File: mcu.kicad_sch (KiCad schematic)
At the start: 24 parts, among them SW1 SW_Push, SW2 SW_Push, U1 RP2040, U2 W25Q128JVS, Y1 Crystal_GND24

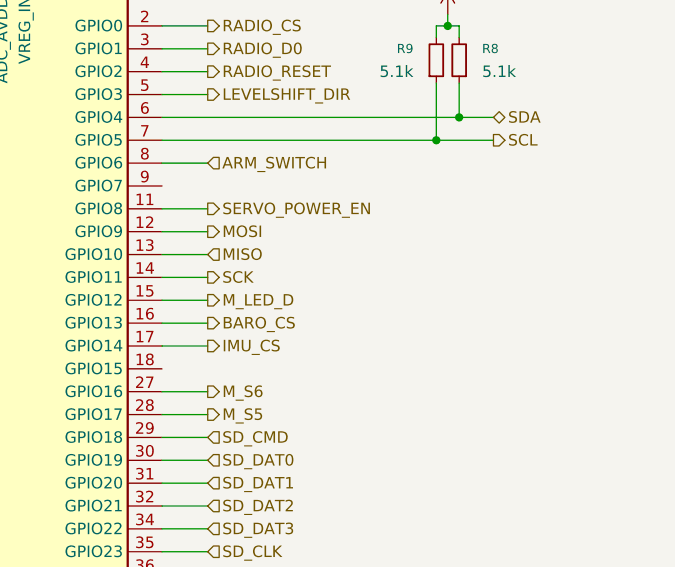
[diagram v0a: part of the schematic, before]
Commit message: switched around some footprints, added expansion header
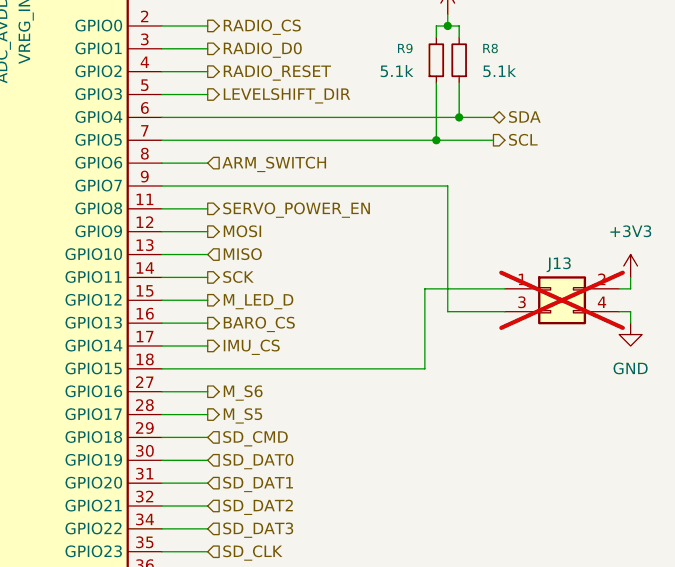
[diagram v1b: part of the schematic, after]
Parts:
- added J13: Conn_02x02_Odd_Even, Connector_PinHeader_1.27mm:PinHeader_2x02_P1.27mm_Vertical, symbol Connector_Generic:Conn_02x02_Odd_Even
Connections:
- net +3V3: now also J13.2 (Pin_2)
- net GND: now also J13.4 (Pin_4)
- net at U1.18 (GPIO15): now also J13.1 (Pin_1)
- net at U1.9 (GPIO7): now also J13.3 (Pin_3)

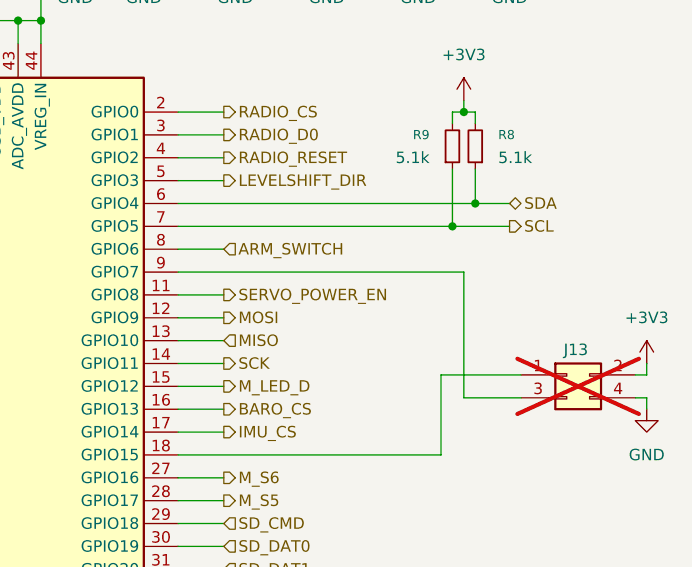
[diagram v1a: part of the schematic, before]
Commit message: switched to global labels for SPI and I2C, added labels for servos
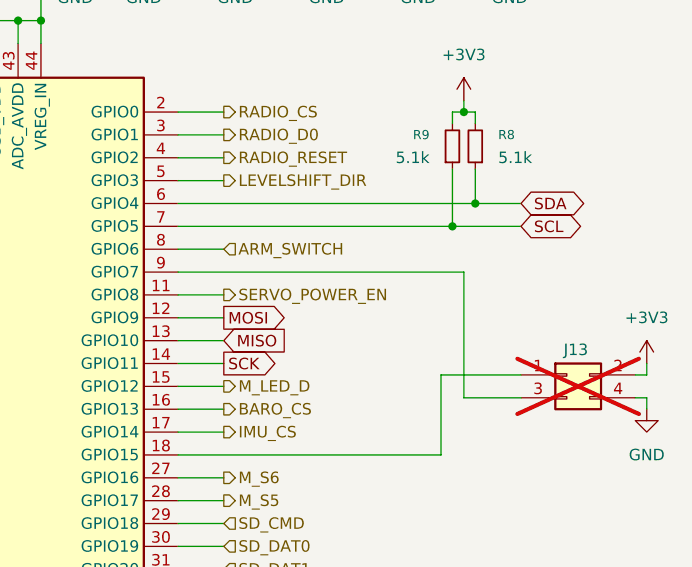
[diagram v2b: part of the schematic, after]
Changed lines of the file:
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@@
 	(wire
 		(pts
-			(xy 226.06 54.61) (xy 229.87 54.61)
+			(xy 226.06 54.61) (xy 231.14 54.61)
 		)
 		(stroke
@@
 	(wire
 		(pts
-			(xy 223.52 57.15) (xy 229.87 57.15)
+			(xy 223.52 57.15) (xy 231.14 57.15)
 		)
 		(stroke
@@
 			)
 			(justify right bottom)
+		)
+	)
+	(global_label "SDA"
+		(shape bidirectional)
+		(at 231.14 54.61 0)
+		(fields_autoplaced yes)
+		(effects
+			(font
+				(size 1.27 1.27)
+			)
+			(justify left)
+		)
+		(property "Intersheetrefs" "${INTERSHEET_REFS}"
+			(at 238.8046 54.61 0)
+			(effects
+				(font
+					(size 1.27 1.27)
+				)
+				(justify left)
+				(hide yes)
+			)
+		)
+	)
+	(global_label "SCK"
+		(shape output)
+		(at 198.12 72.39 0)
+		(fields_autoplaced yes)
+		(effects
+			(font
+				(size 1.27 1.27)
+			)
+			(justify left)
+		)
+		(property "Intersheetrefs" "${INTERSHEET_REFS}"
+			(at 204.8547 72.39 0)
+			(effects
+				(font
+					(size 1.27 1.27)
+				)
+				(justify left)
+				(hide yes)
+			)
+		)
+	)
+	(global_label "SCL"
+		(shape bidirectional)
+		(at 231.14 57.15 0)
+		(fields_autoplaced yes)
+		(effects
+			(font
+				(size 1.27 1.27)
+			)
+			(justify left)
+		)
+		(property "Intersheetrefs" "${INTERSHEET_REFS}"
+			(at 238.7441 57.15 0)
+			(effects
+				(font
+					(size 1.27 1.27)
+				)
+				(justify left)
+				(hide yes)
+			)
+		)
+	)
+	(global_label "MOSI"
+		(shape output)
+		(at 198.12 67.31 0)
+		(fields_autoplaced yes)
+		(effects
+			(font
+				(size 1.27 1.27)
+			)
+			(justify left)
+		)
+		(property "Intersheetrefs" "${INTERSHEET_REFS}"
+			(at 205.7014 67.31 0)
+			(effects
+				(font
+					(size 1.27 1.27)
+				)
+				(justify left)
+				(hide yes)
+			)
+		)
+	)
+	(global_label "MISO"
+		(shape input)
+		(at 198.12 69.85 0)
+		(fields_autoplaced yes)
+		(effects
+			(font
+				(size 1.27 1.27)
+			)
+			(justify left)
+		)
+		(property "Intersheetrefs" "${INTERSHEET_REFS}"
+			(at 205.7014 69.85 0)
+			(effects
+				(font
+					(size 1.27 1.27)
+				)
+				(justify left)
+				(hide yes)
+			)
 		)
 	)
@@
 		)
 	)
-	(hierarchical_label "MOSI"
-		(shape output)
-		(at 198.12 67.31 0)
-		(effects
-			(font
-				(size 1.27 1.27)
-			)
-			(justify left)
-		)
-	)
 	(hierarchical_label "M_S2"
 		(shape output)
@@
 		)
 	)
-	(hierarchical_label "SCK"
-		(shape output)
-		(at 198.12 72.39 0)
-		(effects
-			(font
-				(size 1.27 1.27)
-			)
-			(justify left)
-		)
-	)
 	(hierarchical_label "LEVELSHIFT_DIR"
 		(shape output)
@@
 		)
 	)
-	(hierarchical_label "MISO"
-		(shape input)
-		(at 198.12 69.85 0)
-		(effects
-			(font
-				(size 1.27 1.27)
-			)
-			(justify left)
-		)
-	)
 	(hierarchical_label "M_S6"
 		(shape output)
@@
 		(effects
 			(font
-				(size 1.27 1.27)
-			)
-			(justify left)
-		)
-	)
-	(hierarchical_label "SCL"
-		(shape output)
-		(at 229.87 57.15 0)
-		(effects
-			(font
-				(size 1.27 1.27)
-			)
-			(justify left)
-		)
-	)
-	(hierarchical_label "SDA"
-		(shape bidirectional)
-		(at 229.87 54.61 0)
-		(effects
-			(font

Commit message: add reset pullup...
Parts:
- added R14: 5.1k, Resistor_SMD:R_0402_1005Metric, symbol Device:R_Small
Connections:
- net +3V3: now also R14.2
- net ~{RESET}: now also R14.1
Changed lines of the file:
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@@
 	)
 	(junction
+		(at 124.46 44.45)
+		(diameter 0)
+		(color 0 0 0 0)
+	)
+	(junction
 		(at 153.67 25.4)
 		(diameter 0)
@@
 	(wire
 		(pts
+			(xy 124.46 36.83) (xy 124.46 38.1)
+		)
+		(stroke
+			(width 0)
+			(type default)
+		)
+	)
+	(wire
+		(pts
 			(xy 130.81 77.47) (xy 130.81 64.77)
 		)
@@
 	(wire
 		(pts
+			(xy 124.46 44.45) (xy 142.24 44.45)
+		)
+		(stroke
+			(width 0)
+			(type default)
+		)
+	)
+	(wire
+		(pts
 			(xy 130.81 52.07) (xy 134.62 52.07)
 		)
@@
 	(wire
 		(pts
-			(xy 118.11 44.45) (xy 142.24 44.45)
+			(xy 118.11 44.45) (xy 124.46 44.45)
 		)
 		(stroke
@@
 	(wire
 		(pts
+			(xy 124.46 43.18) (xy 124.46 44.45)
+		)
+		(stroke
+			(width 0)
+			(type default)
+		)
+	)
+	(wire
+		(pts
 			(xy 222.25 73.66) (xy 222.25 82.55)
 		)
@@
 	(symbol
 		(lib_id "Device:R_Small")
+		(at 124.46 40.64 0)
+		(mirror x)
+		(unit 1)
+		(exclude_from_sim no)
+		(in_bom yes)
+		(on_board yes)
+		(dnp no)
+		(property "Reference" "R14"
+			(at 121.92 39.3699 0)
+			(effects
+				(font
+					(size 1.016 1.016)
+				)
+				(justify right)
+			)
+		)
+		(property "Value" "5.1k"
+			(at 121.92 41.9099 0)
+			(effects
+				(font
+					(size 1.27 1.27)
+				)
+				(justify right)
+			)
+		)
+		(property "Footprint" "Resistor_SMD:R_0402_1005Metric"
+			(at 124.46 40.64 0)
+			(effects
+				(font
+					(size 1.27 1.27)
+				)
+				(hide yes)
+			)
+		)
+		(property "Datasheet" "~"
+			(at 124.46 40.64 0)
+			(effects
+				(font
+					(size 1.27 1.27)
+				)
+				(hide yes)
+			)
+		)
+		(property "Description" "Resistor, small symbol"
+			(at 124.46 40.64 0)
+			(effects
+				(font
+					(size 1.27 1.27)
+				)
+				(hide yes)
+			)
+		)
+		(property "LCSC" "C25905"
+			(at 124.46 40.64 0)
+			(effects
+				(font
+					(size 1.27 1.27)
+				)
+				(hide yes)
+			)
+		)
+		(property "digikey" ""
+			(at 124.46 40.64 0)
+			(effects
+				(font
+					(size 1.27 1.27)
+				)
+				(hide yes)
+			)
+		)
+		(pin "2"
+		)
+		(pin "1"
+		)
+		(instances
+			(project "beavs-sketch-0"
+				(path "/49232f62-a438-4b3e-9be5-c2b3074d8de1/41e54b18-0bb2-4af3-8e30-a27cf4650be3"
+					(reference "R14")
+					(unit 1)
+				)
+			)
+		)
+	)
+	(symbol
+		(lib_id "Device:R_Small")
 		(at 223.52 48.26 0)
 		(mirror x)
@@
 					(unit 1)
 				)
+			)
+		)
+	)
+	(symbol
+		(lib_id "power:+3V3")
+		(at 124.46 36.83 0)
+		(unit 1)
+		(exclude_from_sim no)
+		(in_bom yes)
+		(on_board yes)
+		(dnp no)
+		(fields_autoplaced yes)
+		(property "Reference" "#PWR0134"
+			(at 124.46 40.64 0)
+			(effects
+				(font
+					(size 1.27 1.27)
+				)
+				(hide yes)
+			)
+		)
+		(property "Value" "+3V3"
+			(at 124.46 31.75 0)
+			(effects
+				(font
+					(size 1.27 1.27)
+				)
+			)
+		)
+		(property "Footprint" ""
+			(at 124.46 36.83 0)
+			(effects
+				(font
+					(size 1.27 1.27)
+				)
+				(hide yes)
+			)
+		)
+		(property "Datasheet" ""
+			(at 124.46 36.83 0)
+			(effects
+				(font
+					(size 1.27 1.27)
+				)
+				(hide yes)
+			)
+		)
+		(property "Description" "Power symbol creates a global label with name \"+3V3\""
+			(at 124.46 36.83 0)
+			(effects
+				(font
+					(size 1.27 1.27)
+				)
+				(hide yes)
+			)
+		)
+		(pin "1"
+		)
+		(instances
+			(project "beavs-sketch-0"
+				(path "/49232f62-a438-4b3e-9be5-c2b3074d8de1/41e54b18-0bb2-4af3-8e30-a27cf4650be3"
+					(reference "#PWR0134")
+					(unit 1)
+				)

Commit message: various tweaks
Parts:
- added TP1, TP2: TestPoint, TestPoint:TestPoint_Pad_D1.0mm, symbol Connector:TestPoint
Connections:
- net GND: now also U1.19 (TESTEN)
- net at U1.24 (SWCLK): now also TP1.1
- net at U1.25 (SWD): now also TP2.1
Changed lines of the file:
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@@
 	(wire
 		(pts
+			(xy 140.97 120.65) (xy 140.97 121.92)
+		)
+		(stroke
+			(width 0)
+			(type default)
+		)
+	)
+	(wire
+		(pts
 			(xy 175.26 34.29) (xy 175.26 36.83)
 		)
@@
 	(wire
 		(pts
+			(xy 142.24 120.65) (xy 140.97 120.65)
+		)
+		(stroke
+			(width 0)
+			(type default)
+		)
+	)
+	(wire
+		(pts
 			(xy 193.04 72.39) (xy 198.12 72.39)
 		)
@@
 	)
 	(symbol
+		(lib_id "Connector:TestPoint")
+		(at 142.24 110.49 90)
+		(unit 1)
+		(exclude_from_sim no)
+		(in_bom yes)
+		(on_board yes)
+		(dnp no)
+		(fields_autoplaced yes)
+		(property "Reference" "TP1"
+			(at 138.938 105.41 90)
+			(effects
+				(font
+					(size 1.27 1.27)
+				)
+			)
+		)
+		(property "Value" "TestPoint"
+			(at 138.938 107.95 90)
+			(effects
+				(font
+					(size 1.27 1.27)
+				)
+			)
+		)
+		(property "Footprint" "TestPoint:TestPoint_Pad_D1.0mm"
+			(at 142.24 105.41 0)
+			(effects
+				(font
+					(size 1.27 1.27)
+				)
+				(hide yes)
+			)
+		)
+		(property "Datasheet" "~"
+			(at 142.24 105.41 0)
+			(effects
+				(font
+					(size 1.27 1.27)
+				)
+				(hide yes)
+			)
+		)
+		(property "Description" "test point"
+			(at 142.24 110.49 0)
+			(effects
+				(font
+					(size 1.27 1.27)
+				)
+				(hide yes)
+			)
+		)
+		(pin "1"
+		)
+		(instances
+			(project ""
+				(path "/49232f62-a438-4b3e-9be5-c2b3074d8de1/41e54b18-0bb2-4af3-8e30-a27cf4650be3"
+					(reference "TP1")
+					(unit 1)
+				)
+			)
+		)
+	)
+	(symbol
 		(lib_id "power:GND")
 		(at 125.73 102.87 0)
@@
 	)
 	(symbol
+		(lib_id "power:GND")
+		(at 140.97 121.92 0)
+		(unit 1)
+		(exclude_from_sim no)
+		(in_bom yes)
+		(on_board yes)
+		(dnp no)
+		(fields_autoplaced yes)
+		(property "Reference" "#PWR0135"
+			(at 140.97 128.27 0)
+			(effects
+				(font
+					(size 1.27 1.27)
+				)
+				(hide yes)
+			)
+		)
+		(property "Value" "GND"
+			(at 140.97 127 0)
+			(effects
+				(font
+					(size 1.27 1.27)
+				)
+			)
+		)
+		(property "Footprint" ""
+			(at 140.97 121.92 0)
+			(effects
+				(font
+					(size 1.27 1.27)
+				)
+				(hide yes)
+			)
+		)
+		(property "Datasheet" ""
+			(at 140.97 121.92 0)
+			(effects
+				(font
+					(size 1.27 1.27)
+				)
+				(hide yes)
+			)
+		)
+		(property "Description" "Power symbol creates a global label with name \"GND\" , ground"
+			(at 140.97 121.92 0)
+			(effects
+				(font
+					(size 1.27 1.27)
+				)
+				(hide yes)
+			)
+		)
+		(pin "1"
+		)
+		(instances
+			(project ""
+				(path "/49232f62-a438-4b3e-9be5-c2b3074d8de1/41e54b18-0bb2-4af3-8e30-a27cf4650be3"
+					(reference "#PWR0135")
+					(unit 1)
+				)
+			)
+		)
+	)
+	(symbol
 		(lib_id "Device:C_Small")
 		(at 133.35 29.21 0)
@@
 					(unit 1)
 				)
+			)
+		)
+	)
+	(symbol
+		(lib_id "Connector:TestPoint")
+		(at 142.24 113.03 90)
+		(mirror x)
+		(unit 1)
+		(exclude_from_sim no)
+		(in_bom yes)
+		(on_board yes)
+		(dnp no)
+		(property "Reference" "TP2"
+			(at 138.938 118.11 90)
+			(effects
+				(font
+					(size 1.27 1.27)
+				)
+			)
+		)
+		(property "Value" "TestPoint"
+			(at 138.938 115.57 90)
+			(effects
+				(font
+					(size 1.27 1.27)
+				)
+			)
+		)
+		(property "Footprint" "TestPoint:TestPoint_Pad_D1.0mm"
+			(at 142.24 118.11 0)
+			(effects
+				(font
+					(size 1.27 1.27)
+				)
+				(hide yes)
+			)
+		)
+		(property "Datasheet" "~"
+			(at 142.24 118.11 0)
+			(effects
+				(font
+					(size 1.27 1.27)
+				)
+				(hide yes)
+			)
+		)
+		(property "Description" "test point"
+			(at 142.24 113.03 0)
+			(effects
+				(font
+					(size 1.27 1.27)
+				)
+				(hide yes)
+			)
+		)
+		(pin "1"
+		)
+		(instances
+			(project "beavs-sketch-0"
+				(path "/49232f62-a438-4b3e-9be5-c2b3074d8de1/41e54b18-0bb2-4af3-8e30-a27cf4650be3"
+					(reference "TP2")
+					(unit 1)
+				)

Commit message: final tweaks
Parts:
- removed JP1: SolderJumper_2_Bridged, Jumper:SolderJumper-2_P1.3mm_Bridged_RoundedPad1.0x1.5mm, symbol Jumper:SolderJumper_2_Bridged
- added J14: Conn_01x02, Connector_PinHeader_1.27mm:PinHeader_1x02_P1.27mm_Vertical, symbol Connector_Generic:Conn_01x02
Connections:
- net GND: now also J14.1 (Pin_1)
- net at SW1.1, SW2.1: now also J14.2 (Pin_2)
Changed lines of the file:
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@@
 	(wire
 		(pts
+			(xy 102.87 54.61) (xy 106.68 54.61)
+		)
+		(stroke
+			(width 0)
+			(type default)
+		)
+	)
+	(wire
+		(pts
 			(xy 162.56 34.29) (xy 165.1 34.29)
 		)
@@
 	(wire
 		(pts
-			(xy 96.52 54.61) (xy 97.79 54.61)
+			(xy 96.52 54.61) (xy 100.33 54.61)
 		)
 		(stroke
@@
 		)
 	)
-	(wire
-		(pts
-			(xy 105.41 54.61) (xy 106.68 54.61)
-		)
-		(stroke
-			(width 0)
-			(type default)
-		)
-	)
 	(label "~{RESET}"
 		(at 135.89 44.45 180)
@@
 	)
 	(symbol
+		(lib_id "Connector_Generic:Conn_01x02")
+		(at 100.33 49.53 90)
+		(unit 1)
+		(exclude_from_sim no)
+		(in_bom yes)
+		(on_board yes)
+		(dnp no)
+		(property "Reference" "J14"
+			(at 100.33 46.99 90)
+			(effects
+				(font
+					(size 1.27 1.27)
+				)
+				(justify right)
+			)
+		)
+		(property "Value" "Conn_01x02"
+			(at 105.41 50.7999 90)
+			(effects
+				(font
+					(size 1.27 1.27)
+				)
+				(justify right)
+				(hide yes)
+			)
+		)
+		(property "Footprint" "Connector_PinHeader_1.27mm:PinHeader_1x02_P1.27mm_Vertical"
+			(at 100.33 49.53 0)
+			(effects
+				(font
+					(size 1.27 1.27)
+				)
+				(hide yes)
+			)
+		)
+		(property "Datasheet" "~"
+			(at 100.33 49.53 0)
+			(effects
+				(font
+					(size 1.27 1.27)
+				)
+				(hide yes)
+			)
+		)
+		(property "Description" "Generic connector, single row, 01x02, script generated (kicad-library-utils/schlib/autogen/connector/)"
+			(at 100.33 49.53 0)
+			(effects
+				(font
+					(size 1.27 1.27)
+				)
+				(hide yes)
+			)
+		)
+		(pin "1"
+		)
+		(pin "2"
+		)
+		(instances
+			(project ""
+				(path "/49232f62-a438-4b3e-9be5-c2b3074d8de1/41e54b18-0bb2-4af3-8e30-a27cf4650be3"
+					(reference "J14")
+					(unit 1)
+				)
+			)
+		)
+	)
+	(symbol
 		(lib_id "Device:R_Small")
 		(at 124.46 40.64 0)
@@
 					(unit 1)
 				)
-			)
-		)
-	)
-	(symbol
-		(lib_id "Jumper:SolderJumper_2_Bridged")
-		(at 101.6 54.61 0)
-		(unit 1)
-		(exclude_from_sim no)
-		(in_bom no)
-		(on_board yes)
-		(dnp no)
-		(property "Reference" "JP1"
-			(at 101.6 48.26 0)
-			(effects
-				(font
-					(size 1.27 1.27)
-				)
-			)
-		)
-		(property "Value" "SolderJumper_2_Bridged"
-			(at 93.726 50.546 0)
-			(effects
-				(font
-					(size 1.27 1.27)
-				)
-			)
-		)
-		(property "Footprint" "Jumper:SolderJumper-2_P1.3mm_Bridged_RoundedPad1.0x1.5mm"
-			(at 101.6 54.61 0)
-			(effects
-				(font
-					(size 1.27 1.27)
-				)
-				(hide yes)
-			)
-		)
-		(property "Datasheet" "~"
-			(at 101.6 54.61 0)
-			(effects
-				(font
-					(size 1.27 1.27)
-				)
-				(hide yes)
-			)
-		)
-		(property "Description" "Solder Jumper, 2-pole, closed/bridged"
-			(at 101.6 54.61 0)
-			(effects
-				(font
-					(size 1.27 1.27)
-				)
-				(hide yes)
-			)
-		)
-		(property "LCSC" ""
-			(at 101.6 54.61 0)
-			(effects
-				(font
-					(size 1.27 1.27)
-				)
-				(hide yes)
-			)
-		)
-		(property "digikey" ""
-			(at 101.6 54.61 0)
-			(effects
-				(font
-					(size 1.27 1.27)
-				)
-				(hide yes)
-			)
-		)
-		(pin "2"
-		)
-		(pin "1"
-		)
-		(instances
-			(project ""
-				(path "/49232f62-a438-4b3e-9be5-c2b3074d8de1/41e54b18-0bb2-4af3-8e30-a27cf4650be3"
-					(reference "JP1")
-					(unit 1)
-				)

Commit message: blunkinator
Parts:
- J14: digikey (none) -> SAM1156-01-ND
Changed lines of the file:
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@@
+			)
+		)
+		(property "digikey" "SAM1156-01-ND"
+			(at 100.33 49.53 90)
+			(effects
+				(font
+					(size 1.27 1.27)
+				)
+				(hide yes)
 			)
 		)
